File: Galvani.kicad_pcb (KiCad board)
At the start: 4 copper layers, 101.6 x 38.1 mm, 90 parts, among them J1 USB-C Receptacle, J2 U.FL Connector, J3 JST-PH, J4 JST-PH, P1 Cap 1.5pF 0201, P2 L 2.7 nH 0201, P3 Cap 1.5pF 0201, SW1 Pushbutton 4.2x3.2mm 250gf, SW2 Pushbutton 4.2x3.2mm 250gf, U1 LMR14030SDDAR, U2 ESP32-C3FN4, U3 W25Q128JVS, U4 SN74LVC1T45DBVR, U5 TPS560430, U6 SN74LVC1T45DBVR, Y1 Crystal 40MHz 2016

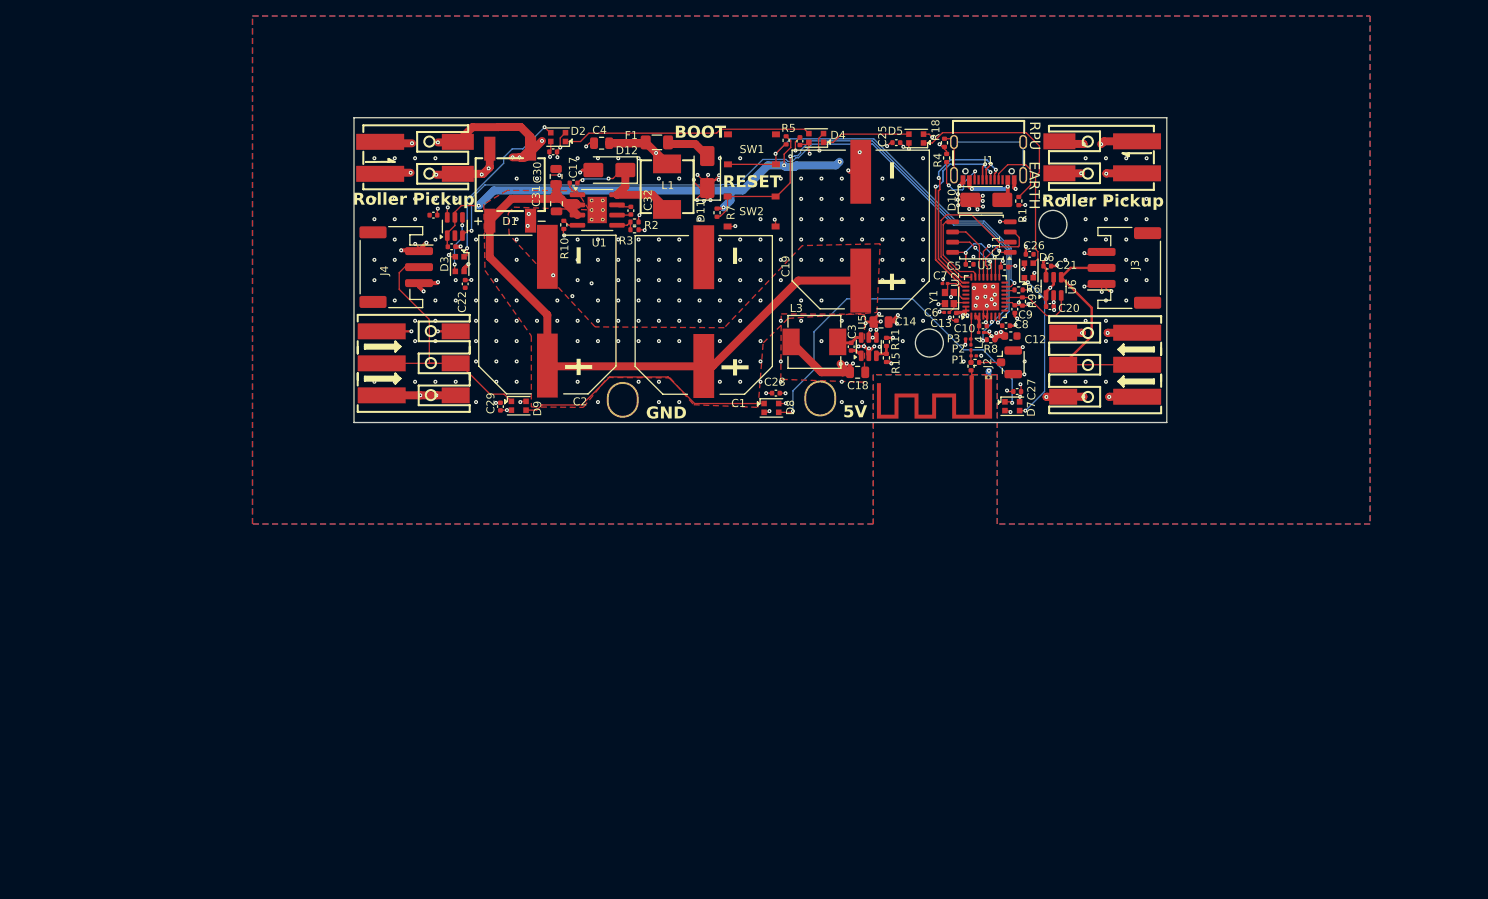
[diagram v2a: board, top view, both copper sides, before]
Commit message: evt2: finish pcb
Signed-off-by: Sean Cross <sean@xobs.io>
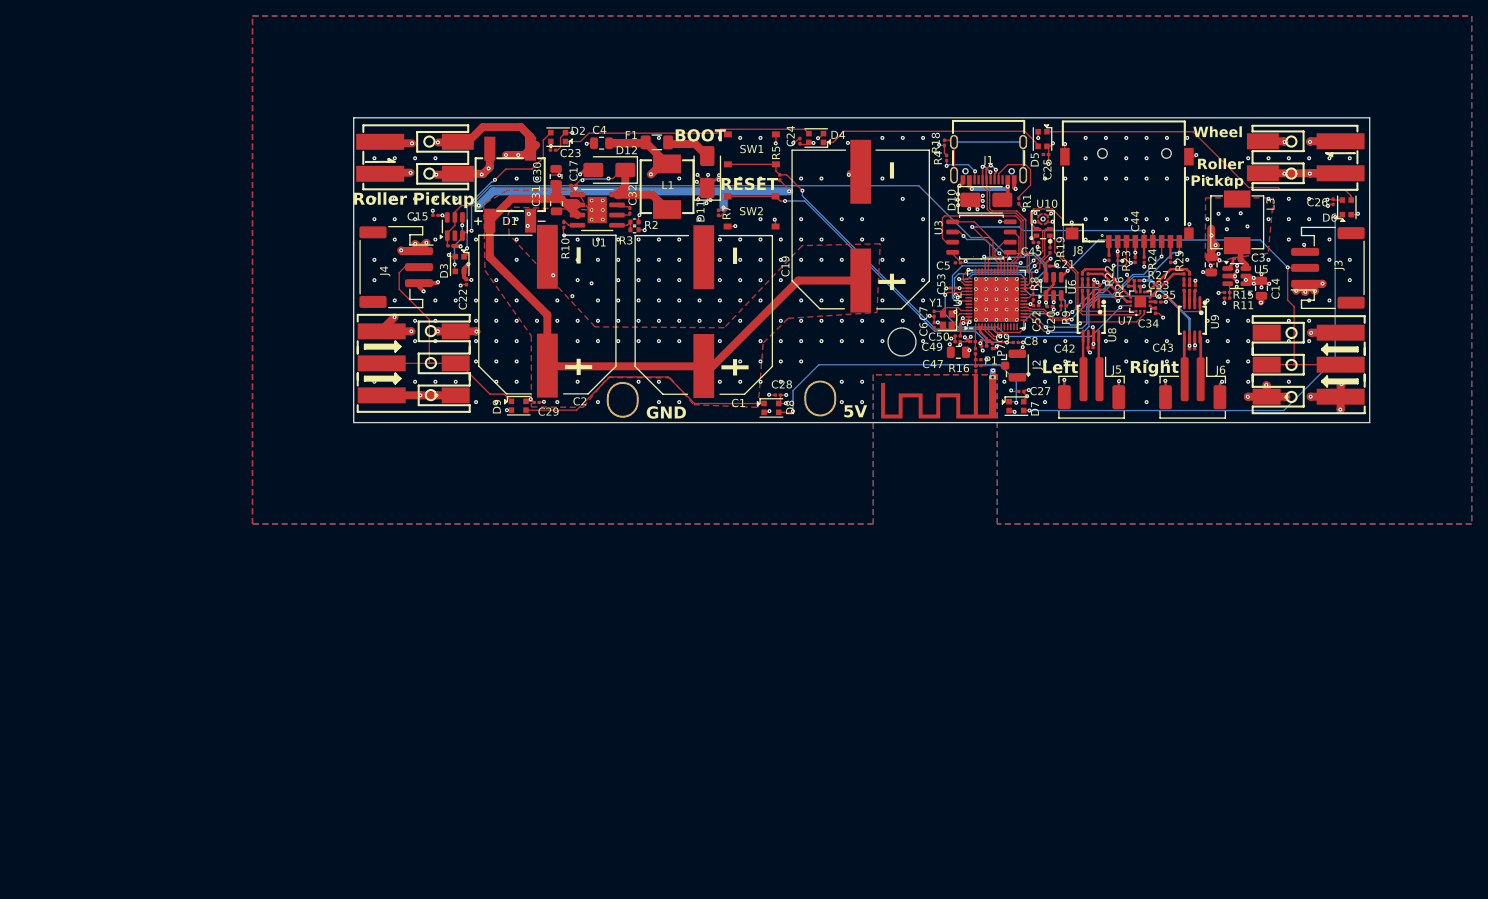
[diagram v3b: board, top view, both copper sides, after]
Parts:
- removed C11: Cap 100nF 0402, Capacitor_SMD:C_0402_1005Metric
- removed C12: Cap 10uF 0603, Capacitor_SMD:C_0603_1608Metric
- removed C13: Cap 10nF 0402, Capacitor_SMD:C_0402_1005Metric
- removed H3: Mounting Hole, MountingHole:MountingHole_3.5mm
- removed L4: L 2.7 nH 0201, Inductor_SMD:L_0201_0603Metric
- added C33: Cap 1uF 0201, Galvani:C_0201_0603Metric, F.Cu at (178.2, 104.2)
- added C34: Cap 1uF 0201, Galvani:C_0201_0603Metric, F.Cu at (180.5, 107.3)
- added C35: Cap 1uF 0201, Galvani:C_0201_0603Metric, F.Cu at (180.8, 106.2)
- added C36: Cap 1uF 0201, Galvani:C_0201_0603Metric, F.Cu at (172.1, 103.0)
- added C37: Cap 1uF 0201, Galvani:C_0201_0603Metric, F.Cu at (171.3, 103.0)
- added C38: Cap 1uF 0201, Galvani:C_0201_0603Metric, F.Cu at (184.8, 103.0)
- added C39: Cap 1uF 0201, Galvani:C_0201_0603Metric, F.Cu at (184.0, 103.0)
- added C40: Cap 1uF 0201, Galvani:C_0201_0603Metric, F.Cu at (172.8, 104.4)
- added C41: Cap 1uF 0201, Galvani:C_0201_0603Metric, F.Cu at (185.5, 104.4)
- added C42: Cap 100nF 0201, Galvani:C_0201_0603Metric, F.Cu at (172.4, 111.9)
- added C43: Cap 100nF 0201, Galvani:C_0201_0603Metric, F.Cu at (185.1, 112.1)
- added C44: Cap 100nF 0201, Galvani:C_0201_0603Metric, F.Cu at (178.0, 100.9)
- added C45: Cap 1uF 0201, Galvani:C_0201_0603Metric, F.Cu at (165.6, 98.8)
- added C47: Cap 10uF 0805, Capacitor_SMD:C_0805_2012Metric, F.Cu at (155.8, 112.5)
- added C49: Cap 1uF 0201, Galvani:C_0201_0603Metric, F.Cu at (155.8, 111.2)
- added C50: Cap 100nF 0201, Galvani:C_0201_0603Metric, F.Cu at (155.8, 110.5)
- added C51: Cap 100nF 0201, Galvani:C_0201_0603Metric, F.Cu at (159.1, 111.7)
- added C52: Cap 100nF 0201, Galvani:C_0201_0603Metric, F.Cu at (165.6, 106.7)
- added C53: Cap 100nF 0201, Galvani:C_0201_0603Metric, F.Cu at (155.2, 104.5)
- added J5: JST PH2.0-1x2, Galvani:JST_PH_B2B-PH-SM4-TB_1x02-1MP_P2.00mm_Vertical, F.Cu at (172.5, 116.4)
- added J6: JST PH2.0-1x2, Galvani:JST_PH_B2B-PH-SM4-TB_1x02-1MP_P2.00mm_Vertical, F.Cu at (185.1, 116.4)
- added J8: Micro SD Card, Galvani:TF-SMD_TF-PUSH, F.Cu at (176.9, 93.3)
- added P7: L 2.7nH 0201, Inductor_SMD:L_0201_0603Metric, F.Cu at (160.1, 111.7)
- added R12: R 20k 0201, Galvani:R_0201_0603Metric, F.Cu at (171.3, 104.5)
- added R13: R 20k 0201, Galvani:R_0201_0603Metric, F.Cu at (184.8, 104.4)
- added R14: R 20k 0201, Galvani:R_0201_0603Metric, F.Cu at (184.0, 104.4)
- added R19: R 0 ohm 0201, Galvani:R_0201_0603Metric, F.Cu at (167.3, 99.7)
- added R21: R 20k 0201, Galvani:R_0201_0603Metric, F.Cu at (172.1, 104.5)
- added R22: R 20k 0201, Galvani:R_0201_0603Metric, F.Cu at (174.7, 100.7)
- added R23: R 20k 0201, Galvani:R_0201_0603Metric, F.Cu at (175.8, 100.7)
- added R24: R 20k 0201, Galvani:R_0201_0603Metric, F.Cu at (179.1, 100.9)
- added R25: R 20k 0201, Galvani:R_0201_0603Metric, F.Cu at (182.4, 100.9)
- added R26: R 0 ohm 0201, Galvani:R_0201_0603Metric, F.Cu at (177.1, 103.9)
- added R27: R 0 ohm 0201, Galvani:R_0201_0603Metric, F.Cu at (178.2, 103.5)
- added U10: MEMS Microphone, Galvani:RHLGA-5L_L3.5-W2.7-P0.82-MP23ABS1TR, F.Cu at (166.4, 96.6)
- added U7: ES7149, Galvani:QFN-12_L2.5-W2.5-P0.50-BL-EP, F.Cu at (178.6, 106.2)
- added U8: NS4150, Galvani:MSOP-8_L3.0-W3.0-P0.65-LS5.0-BL, F.Cu at (172.4, 108.4)
- added U9: NS4150, Galvani:MSOP-8_L3.0-W3.0-P0.65-LS5.0-BL, F.Cu at (185.1, 108.4)
- C10, C9: value Cap 1uF 0402 -> Cap 100nF 0201; footprint Capacitor_SMD:C_0402_1005Metric -> Galvani:C_0201_0603Metric
- C15, C16, C17, C20, C21, C22, C23, C24, C25, C26, C27, C28, C29, C3, C5: value Cap 100nF 0402 -> Cap 100nF 0201; footprint Capacitor_SMD:C_0402_1005Metric -> Galvani:C_0201_0603Metric
- C32: value Cap 10nF 0402 -> Cap 10nF 0201; footprint Capacitor_SMD:C_0402_1005Metric -> Galvani:C_0201_0603Metric
- C6, C7: footprint Capacitor_SMD:C_0201_0603Metric -> Galvani:C_0201_0603Metric
- C8: value Cap 1uF 0402 -> Cap 1uF 0201; footprint Capacitor_SMD:C_0402_1005Metric -> Galvani:C_0201_0603Metric
- J3, J4: value JST-PH -> JST-PH-1x3
- P1: value Cap 1.5pF 0201 -> Cap 2.4pF 0201; footprint Capacitor_SMD:C_0201_0603Metric -> Galvani:C_0201_0603Metric
- P2: value L 2.7 nH 0201 -> L 2.7nH 0201
- P3: value Cap 1.5pF 0201 -> Cap 3.9pF 0201; footprint Capacitor_SMD:C_0201_0603Metric -> Galvani:C_0201_0603Metric
- R1, R4: value R 5.1k 0402 -> R 5.1k 0201; footprint Resistor_SMD:R_0402_1005Metric -> Galvani:R_0201_0603Metric
- R10, R5, R6, R7, R8, R9: value R 20k 0402 -> R 20k 0201; footprint Resistor_SMD:R_0402_1005Metric -> Galvani:R_0201_0603Metric
- R11: value R 22.1k 0402 -> R 22.1k 0201; footprint Resistor_SMD:R_0402_1005Metric -> Galvani:R_0201_0603Metric
- R15: value R 20k 0402 -> R 51k 0201; footprint Resistor_SMD:R_0402_1005Metric -> Galvani:R_0201_0603Metric
- R16, R17, R18: value R 20k 0402 -> R 0 ohm 0201; footprint Resistor_SMD:R_0402_1005Metric -> Galvani:R_0201_0603Metric
- R2: value R 20k 0402 -> R 68k 0402
- R3: value R 20k 0402 -> R 12k 0402
- SW1, SW2: footprint Button_Switch_SMD:SW_Push_1P1T_XKB_TS-1187A -> Galvani:SW_Push_1P1T_XKB_TS-1187A
- TP1: value GND -> 5V
- TP2: value 5V -> GND
- U2: value ESP32-C3FN4 -> ESP32-S3; footprint Package_DFN_QFN:QFN-32-1EP_5x5mm_P0.5mm_EP3.45x3.45mm -> Package_DFN_QFN:QFN-56-1EP_7x7mm_P0.4mm_EP5.6x5.6mm_ThermalVias
- moved L3 54.9 mm to (190.7, 96.2), turned to 90 degrees
- moved C3 49.4 mm to (190.7, 100.8), turned to 180 degrees
- moved C14 47.7 mm to (193.7, 104.5), turned to -90 degrees
- moved U5 46.8 mm to (190.7, 103.0), turned to 0 degrees
- moved C18 46.2 mm to (187.5, 101.6), turned to -90 degrees
- moved R15 43.4 mm to (189.4, 105.0), turned to 180 degrees
- moved R11 42.9 mm to (189.4, 105.7), turned to 180 degrees
- moved D6 40.5 mm to (204.4, 94.4)
- moved C26 38.5 mm to (202.7, 93.7), turned to -90 degrees
- moved CONN1 25.4 mm to (199.0, 114.0)
- moved CONN3 25.4 mm to (198.8, 88.1)
- moved J3 25.4 mm to (202.0, 101.9)
- moved C25 18.8 mm to (166.8, 87.8)
- moved D5 15.8 mm to (166.4, 85.8), turned to -90 degrees
- moved R6 10.1 mm to (173.5, 104.4), turned to 90 degrees
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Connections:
- net /5V_UNFUSED renamed /Heirarchy/Power/5V_UNFUSED
- net /LED_EXTERNAL_5V renamed /Heirarchy/LEDs/LED_EXTERNAL_5V
- net /LED_INTERNAL_5V renamed /Heirarchy/LEDs/LED_INTERNAL_5V
- net /USB_INT_DN renamed /Heirarchy/CPU/USB_INT_DN
- net /USB_INT_DP renamed /Heirarchy/CPU/USB_INT_DP
- net /VAC_RECTIFIED renamed /Heirarchy/Power/VAC_RECTIFIED
- C10 pad 1: Net-(C10-Pad1) -> VWIFI
- C15 pad 1: GND -> V5V
- C15 pad 2: VWIFI -> GND
- C16 pad 1: V5V -> GND
- C16 pad 2: GND -> VWIFI
- C6 pad 1: Net-(U2-XTAL_P) -> /Heirarchy/CPU/XTAL_P
- C7 pad 2: Net-(U2-XTAL_N) -> /Heirarchy/CPU/XTAL_N
- C8 pad 1: /RESET -> /Heirarchy/CPU/RESET
- C9 pad 1: VWIFI -> /Heirarchy/CPU/ESP32_VDD3P3
- R5 pad 2: /BOOT_MODE -> /Heirarchy/CPU/BOOT_MODE
- R6 pad 1: Net-(U2-GPIO8) -> /Heirarchy/Audio/AUDIO_EN
- R6 pad 2: VWIFI -> GND
- R7 pad 2: /RESET -> /Heirarchy/CPU/RESET
- R8 pad 2: /LED_INTERNAL -> /Heirarchy/CPU/LED_INTERNAL
- R9 pad 2: /LED_EXTERNAL -> /Heirarchy/CPU/LED_EXTERNAL
- SW1 pad 2: /BOOT_MODE -> /Heirarchy/CPU/BOOT_MODE
- SW2 pad 2: /RESET -> /Heirarchy/CPU/RESET
- TP1 pad 1: GND -> V5V
- TP2 pad 1: V5V -> GND
- U2 pad 11: VWIFI -> unconnected-(U2-GPIO6/ADC1_CH5-Pad11)
- U2 pad 12: /LED_EXTERNAL -> unconnected-(U2-GPIO7/ADC1_CH6-Pad12)
- U2 pad 14: Net-(U2-GPIO8) -> unconnected-(U2-GPIO9/ADC1_CH8-Pad14)
- U2 pad 15: /BOOT_MODE -> unconnected-(U2-GPIO10/ADC1_CH9-Pad15)
- U2 pad 16: unconnected-(U2-GPIO10-Pad16) -> /Heirarchy/CPU/SD_DET
- U2 pad 17: VWIFI -> /Heirarchy/CPU/SD_CIPO
- U2 pad 18: VSPI -> /Heirarchy/CPU/SD_CS
- U2 pad 19: /SPI_IO3 -> /Heirarchy/CPU/SD_COPI
- U2 pad 2: Net-(C10-Pad1) -> /Heirarchy/CPU/ESP32_VDD3P3
- U2 pad 20: /SPI_IO2 -> VWIFI
- U2 pad 21: /SPI_CS -> unconnected-(U2-GPIO15/ADC2_CH4/XTAL_32K_P-Pad21)
- U2 pad 22: /SPI_CLK -> /Heirarchy/CPU/LED_INTERNAL
- U2 pad 23: /SPI_IO0 -> unconnected-(U2-GPIO17/ADC2_CH6/DAC_2-Pad23)
- U2 pad 24: /SPI_IO1 -> unconnected-(U2-GPIO18/ADC2_CH7/DAC_1-Pad24)
- U2 pad 29: Net-(U2-XTAL_N) -> VSPI
- U2 pad 3: Net-(C10-Pad1) -> /Heirarchy/CPU/ESP32_VDD3P3
- U2 pad 30: Net-(U2-XTAL_P) -> /Heirarchy/CPU/SPI_IO3
- U2 pad 31: VWIFI -> /Heirarchy/CPU/SPI_IO2
- U2 pad 32: VWIFI -> /Heirarchy/CPU/SPI_CS
- U2 pad 33: GND -> /Heirarchy/CPU/SPI_CLK
- U2 pad 4: GND -> /Heirarchy/CPU/RESET
- U2 pad 5: GND -> /Heirarchy/CPU/BOOT_MODE
- U2 pad 6: /LED_INTERNAL -> unconnected-(U2-GPIO1/ADC1_CH0-Pad6)
- U2 pad 7: /RESET -> /Heirarchy/CPU/LED_EXTERNAL
- U3 pad 1: /SPI_CS -> /Heirarchy/CPU/SPI_CS
- U3 pad 2: /SPI_IO1 -> /Heirarchy/CPU/SPI_IO1
- U3 pad 3: /SPI_IO2 -> /Heirarchy/CPU/SPI_IO2
- U3 pad 5: /SPI_IO0 -> /Heirarchy/CPU/SPI_IO0
- U3 pad 6: /SPI_CLK -> /Heirarchy/CPU/SPI_CLK
- U3 pad 7: /SPI_IO3 -> /Heirarchy/CPU/SPI_IO3
- U4 pad 3: /LED_INTERNAL -> /Heirarchy/CPU/LED_INTERNAL
- U6 pad 3: /LED_EXTERNAL -> /Heirarchy/CPU/LED_EXTERNAL
- Y1 pad 1: Net-(U2-XTAL_P) -> /Heirarchy/CPU/XTAL_P
- Y1 pad 3: Net-(U2-XTAL_N) -> /Heirarchy/CPU/XTAL_N
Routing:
- net /LED_INTERNAL: track 95.2 -> 0.00 mm, vias 3 -> 0
- net /Heirarchy/CPU/LED_INTERNAL: track 0.00 -> 87.2 mm, vias 0 -> 2
- net VWIFI: track 190.4 -> 113.4 mm, vias 19 -> 29
- net /RESET: track 60.3 -> 0.00 mm, vias 2 -> 0
- net /Heirarchy/CPU/RESET: track 0.00 -> 51.0 mm, vias 0 -> 2
- net /BOOT_MODE: track 50.8 -> 0.00 mm, vias 2 -> 0
- net /Heirarchy/Audio/I2S_BCLK: track 0.00 -> 47.6 mm, vias 0 -> 2
- net /Heirarchy/CPU/BOOT_MODE: track 0.00 -> 46.1 mm, vias 0 -> 2
- net Net-(D6-DOUT): track 19.3 -> 60.4 mm
- net V5V: track 71.8 -> 111.4 mm, vias 50 -> 56
- net /Heirarchy/Audio/AUDIO_EN: track 0.00 -> 39.5 mm, vias 0 -> 4
- net /Heirarchy/Audio/I2S_LRCK: track 0.00 -> 36.8 mm, vias 0 -> 2
- net /Heirarchy/CPU/SD_CLK: track 0.00 -> 31.5 mm, vias 0 -> 2
- net /Heirarchy/Audio/I2S_OUT: track 0.00 -> 31.5 mm, vias 0 -> 2
- net Earth: track 110.2 -> 141.3 mm
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- added copper zone on In2.Cu, net VWIFI
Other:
- board size 101.6 x 38.1 mm -> 127 x 38.1 mm
- board text added: "Left"
- board text added: "Onboard LEDs are connected to GPIO16 External LEDs are connected to GPIO2 Hold BOOT while pressing RESET to program"
- board text added: "Right"
- board text added: "Wheel"
- board text removed: "EARTH"
- board text removed: "Onboard LEDs are connected to GPIO2 External LEDs are connected to GPIO6 Hold BOOT while pressing RESET to program"
- board text removed: "RPU"

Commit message: release evt2
Signed-off-by: Sean Cross <sean@xobs.io>
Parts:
- removed J3, J4: JST-PH-1x3, Connector_JST:JST_PH_S3B-PH-SM4-TB_1x03-1MP_P2.00mm_Horizontal
- removed kibuzzard-66F0D9BF: G***, kibuzzard-66F0D9BF
- added JP1: Fuse Bypass, Jumper:SolderJumper-2_P1.3mm_Open_TrianglePad1.0x1.5mm, F.Cu at (128.7, 89.1)
- added JP2: Fuse Bypass, Jumper:SolderJumper-2_P1.3mm_Open_TrianglePad1.0x1.5mm, F.Cu at (129.1, 92.6)
- added R20: R 140k 0201, Galvani:R_0201_0603Metric, F.Cu at (109.4, 96.9)
- added R28: R 34k 0201, Galvani:R_0201_0603Metric, F.Cu at (110.1, 96.9)
- added kibuzzard-67065BC0: G***, kibuzzard-67065BC0, B.Cu at (141.9, 96.5)
- D2, D3, D4, D5, D6, D7, D8, D9: value WS2812C-2020 -> WS2812B-2020
- R10, R12, R13, R14, R21, R22, R23, R24, R25, R5, R6, R7, R8, R9: value R 20k 0201 -> R 22.1k 0201
- R2: value R 68k 0402 -> R 68k 0201; footprint Resistor_SMD:R_0402_1005Metric -> Galvani:R_0201_0603Metric
- R3: value R 12k 0402 -> R 12k 0201; footprint Resistor_SMD:R_0402_1005Metric -> Galvani:R_0201_0603Metric
- moved R7 75.8 mm to (201.6, 96.7), turned to 0 degrees
- moved SW2 74.0 mm to (203.7, 100.8), turned to -90 degrees
- moved SW1 48.4 mm to (83.6, 100.7), turned to 90 degrees
- moved R5 48.2 mm to (85.6, 96.6), turned to 180 degrees
- moved F1 10.9 mm to (129.0, 86.6)
- moved D6 10.1 mm to (196.9, 101.2)
- moved C4 8.86 mm to (120.1, 86.9)
- moved D11 8.07 mm to (132.2, 92.3)
- moved C26 8.01 mm to (197.0, 99.3), turned to 0 degrees
- moved D1 4.93 mm to (104.7, 91.5)
- moved C30 4.64 mm to (110.2, 90.9)
- moved C31 4.59 mm to (110.2, 94.4)
- moved R10 4.33 mm to (110.8, 96.9)
- moved C22 4.27 mm to (90.5, 102.0), turned to 180 degrees
- moved C17 4.22 mm to (112.0, 91.6)
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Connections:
- CONN1 pad 1: V5V -> GND
- CONN1 pad 3: GND -> V5V
- CONN2 pad 1: V5V -> GND
- CONN2 pad 3: GND -> V5V
- TP1 pad 1: V5V -> GND
- TP2 pad 1: GND -> V5V
- U1 pad 3: /Heirarchy/Power/VAC_RECTIFIED -> Net-(U1-EN)
- U2 pad 14: unconnected-(U2-GPIO9/ADC1_CH8-Pad14) -> /Heirarchy/Audio/I2S_OUT
- U2 pad 15: unconnected-(U2-GPIO10/ADC1_CH9-Pad15) -> /Heirarchy/Audio/I2S_MCLK
- U2 pad 43: unconnected-(U2-GPIO38-Pad43) -> /Heirarchy/Audio/I2S_LRCK
- U2 pad 44: /Heirarchy/Audio/I2S_LRCK -> /Heirarchy/Audio/I2S_IN
- U2 pad 45: /Heirarchy/Audio/I2S_MCLK -> /Heirarchy/Audio/I2S_BCLK
- U2 pad 47: /Heirarchy/Audio/I2S_OUT -> unconnected-(U2-MTDI/JTAG/GPIO41-Pad47)
- U2 pad 48: /Heirarchy/Audio/I2S_IN -> unconnected-(U2-MTMS/JTAG/GPIO42-Pad48)
- U2 pad 50: /Heirarchy/Audio/I2S_BCLK -> unconnected-(U2-U0RXD/PROG/GPIO44-Pad50)
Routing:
- net /Heirarchy/CPU/BOOT_MODE: track 46.1 -> 87.7 mm
- net /Heirarchy/Audio/I2S_OUT: track 31.5 -> 16.4 mm
- net Net-(D9-DOUT): track 34.1 -> 19.3 mm
- net /Heirarchy/Audio/I2S_MCLK: track 30.7 -> 16.5 mm
- net VWIFI: track 113.4 -> 126.6 mm
- net GND: track 100.1 -> 111.5 mm, vias 356 -> 566
- net Earth: track 141.3 -> 150.1 mm
- net Net-(D11-A): track 5.61 -> 14.0 mm
- net /Heirarchy/CPU/LED_INTERNAL: track 87.2 -> 80.3 mm
- net /Heirarchy/CPU/RESET: track 51.0 -> 57.3 mm
- net Net-(D2-DIN): track 21.7 -> 27.0 mm
- net Net-(D2-DOUT): track 31.3 -> 26.6 mm
- net V5V: track 111.4 -> 107.1 mm, vias 56 -> 43
- net /Heirarchy/Audio/I2S_IN: track 17.7 -> 13.6 mm
- net /Heirarchy/Audio/AUDIO_EN: track 39.5 -> 35.5 mm
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- added copper zone on In2.Cu, net /Heirarchy/Power/VAC_RECTIFIED
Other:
- outline, holes or cut-outs redrawn
- board text added: "Power Input"
- board text added: "RPU"
- board text added: "S"
